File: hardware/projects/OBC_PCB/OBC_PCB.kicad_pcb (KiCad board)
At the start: 8 copper layers, 42.2 x 67.2 mm, 136 parts, among them J1 LS021B7DD02, J2 DM3CS-SF, J3 FH12-12S-0.5SH(55), J4 1S Li-Po, J5 TC2030-CTX-NL, J7 RF coax pads, J8 RF coax pads, Q1 AO3400A, SW1 PREV, SW2 NEXT, SW3 SELECT / POWER, SW4 BACK, U1 MAX-F11N, U2 NPM1300-CAAA-R, U3 BMA400, U4 BMM350, U5 BMP581, U6 nRF54LM20A-PAAA, U7 TPS610997, Y1 32MHz, Y3 32.768kHz

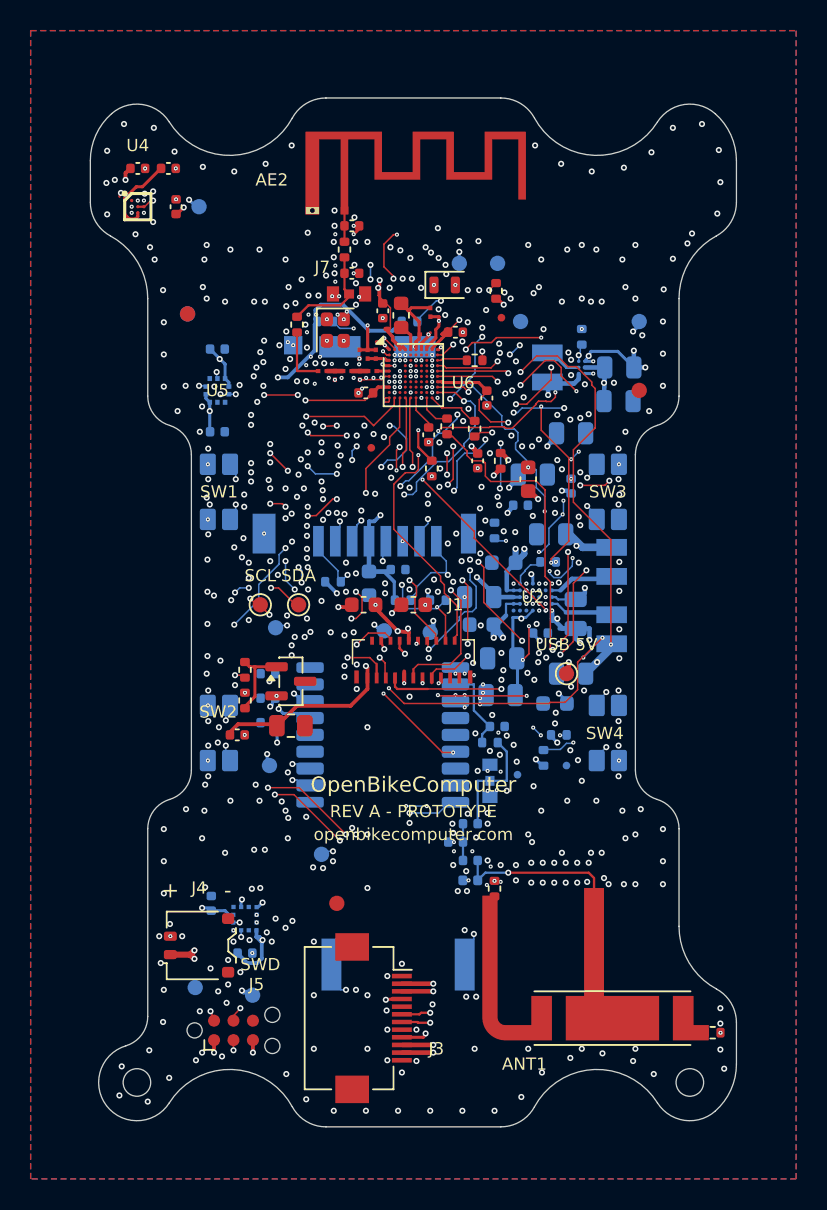
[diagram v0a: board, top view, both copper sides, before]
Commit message: hardware: remove the BGA routing and keep the placement reference
The routed board belongs to the BGA/CSP98 and HDI design. The QFN
redesign replaces it. Remove 1,711 track segments, 993 vias and the
filled copper of the zones.

Keep the placement of all 136 footprints, the board outline, the holes,
the cradle slots and the zone definitions. All other items in the file
are unchanged. The routed board stays in the history, for example at
1e42f5fb5.

The project and rule files keep the HDI settings. The layout redo
replaces them.

Co-Authored-By: Claude Sonnet 5.5 <noreply@anthropic.com>
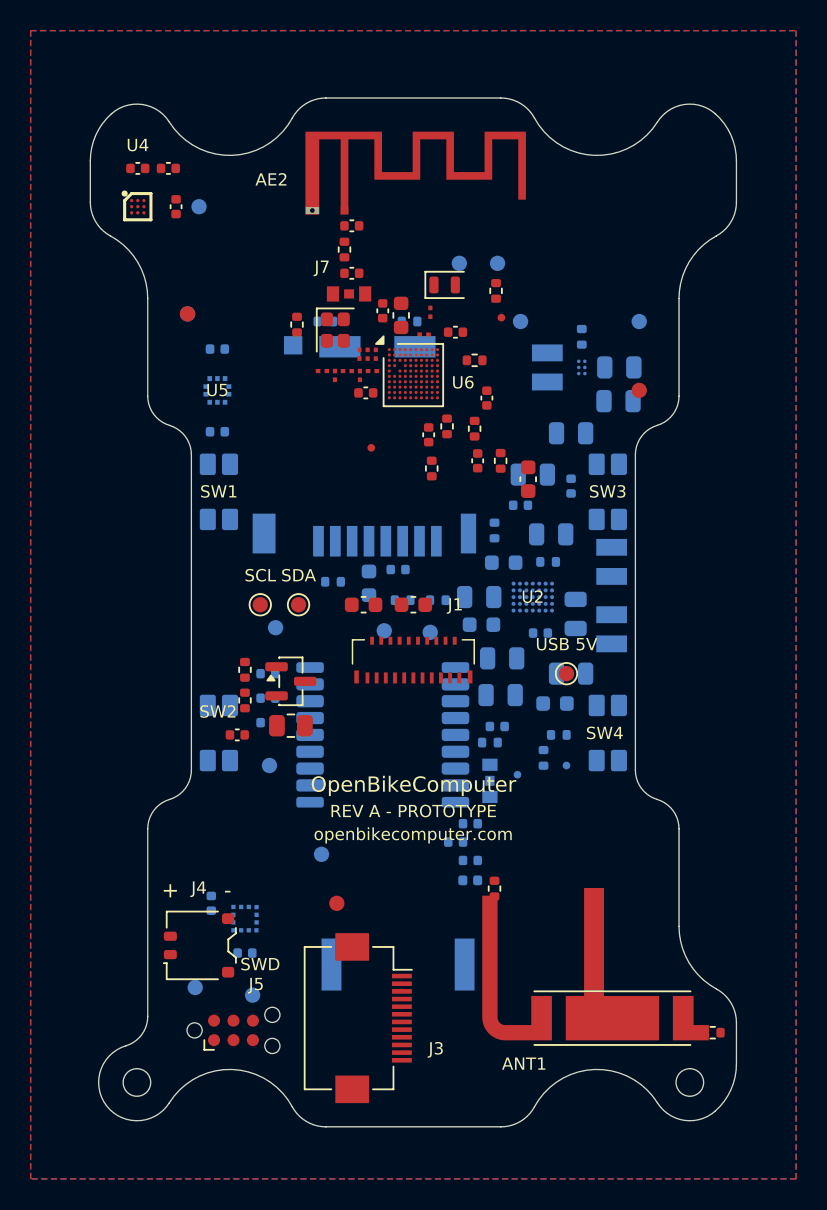
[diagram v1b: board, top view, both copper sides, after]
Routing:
- net /SDA: track 141.6 -> 0.00 mm, vias 36 -> 0
- net /SCL: track 136.9 -> 0.00 mm, vias 32 -> 0
- net /FLPR.P00: track 83.7 -> 0.00 mm, vias 7 -> 0
- net +3V3_SD: track 74.0 -> 0.00 mm, vias 11 -> 0
- net /nRESET: track 71.6 -> 0.00 mm, vias 6 -> 0
- net /Display/FLPR.P05: track 66.3 -> 0.00 mm, vias 14 -> 0
- net Net-(BZ1-~-Pad1): track 62.4 -> 0.00 mm, vias 9 -> 0
- net /SWDIO: track 59.7 -> 0.00 mm, vias 4 -> 0
- net /Power Management/USB_CC1: track 57.1 -> 0.00 mm, vias 8 -> 0
- net /FLPR.P04: track 55.7 -> 0.00 mm, vias 8 -> 0
- net /Display/FLPR.P10: track 54.6 -> 0.00 mm, vias 11 -> 0
- net +1V8_MAG: track 54.0 -> 0.00 mm, vias 6 -> 0
- net /Display/FLPR.P09: track 53.1 -> 0.00 mm, vias 11 -> 0
- net /Display/LCD.VCOM: track 53.0 -> 0.00 mm, vias 11 -> 0
- net /SWDCLK: track 52.7 -> 0.00 mm, vias 9 -> 0
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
